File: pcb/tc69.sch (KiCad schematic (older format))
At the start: 99 parts, among them SW1 ESC, SW10 LWIN, SW11 2, SW12 W, SW13 S, SW14 Z, SW16 3, SW17 E, SW18 D, SW19 X, SW2 TAB, SW20 LALT, SW21 4, SW22 R, SW23 F, SW24 C, SW26 5, SW27 T, SW28 G, SW29 V, SW3 CAPS, SW30 LSPC, SW31 6, SW32 Y, SW33 H, SW34 B, SW36 7, SW37 U, SW38 J, SW39 N, SW4 LSHFT, SW41 8, SW42 I, SW43 K, SW44 M, SW45 RSPC, SW46 9, SW47 O, SW48 L, SW49 COMMA, SW5 LCTRL, SW51 0, SW52 P, SW53 SCLN, SW54 DOT, SW55 RALT, SW56 MINUS, SW57 LBRC, SW58 QUOTE, SW59 SLSH, SW6 1, SW60 RWIN, SW61 EQUAL, SW62 RBRC, SW65 APP, SW66 BS, SW68 ENTER, SW69 RSHFT, SW7 Q, SW70 LEFT, SW72 BSLSH, SW74 UP, SW75 DOWN, SW76 HOME, SW77 PGUP, SW78 PGDN, SW79 END, SW8 A, SW80 RIGHT, U1 SeeeduinoXIAO, U2 74AHC1G04, U3 NCS2003SN2T1G, U4 4051, U5 4051

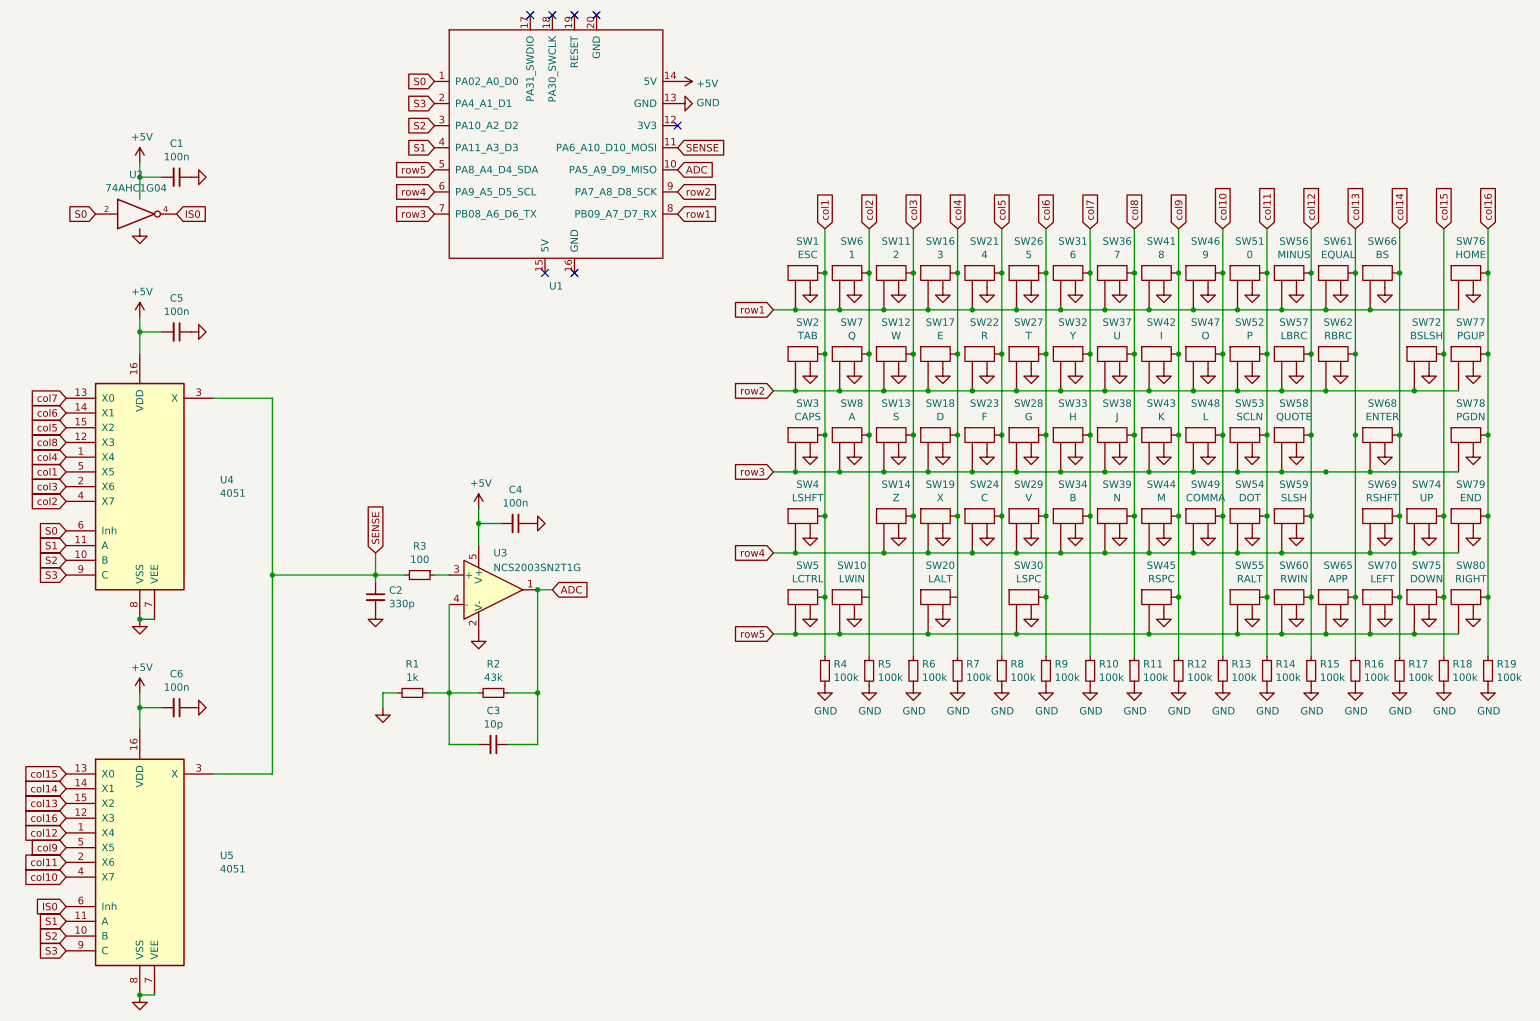
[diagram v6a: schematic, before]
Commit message: fix power line, made xiao rp2040 compatible
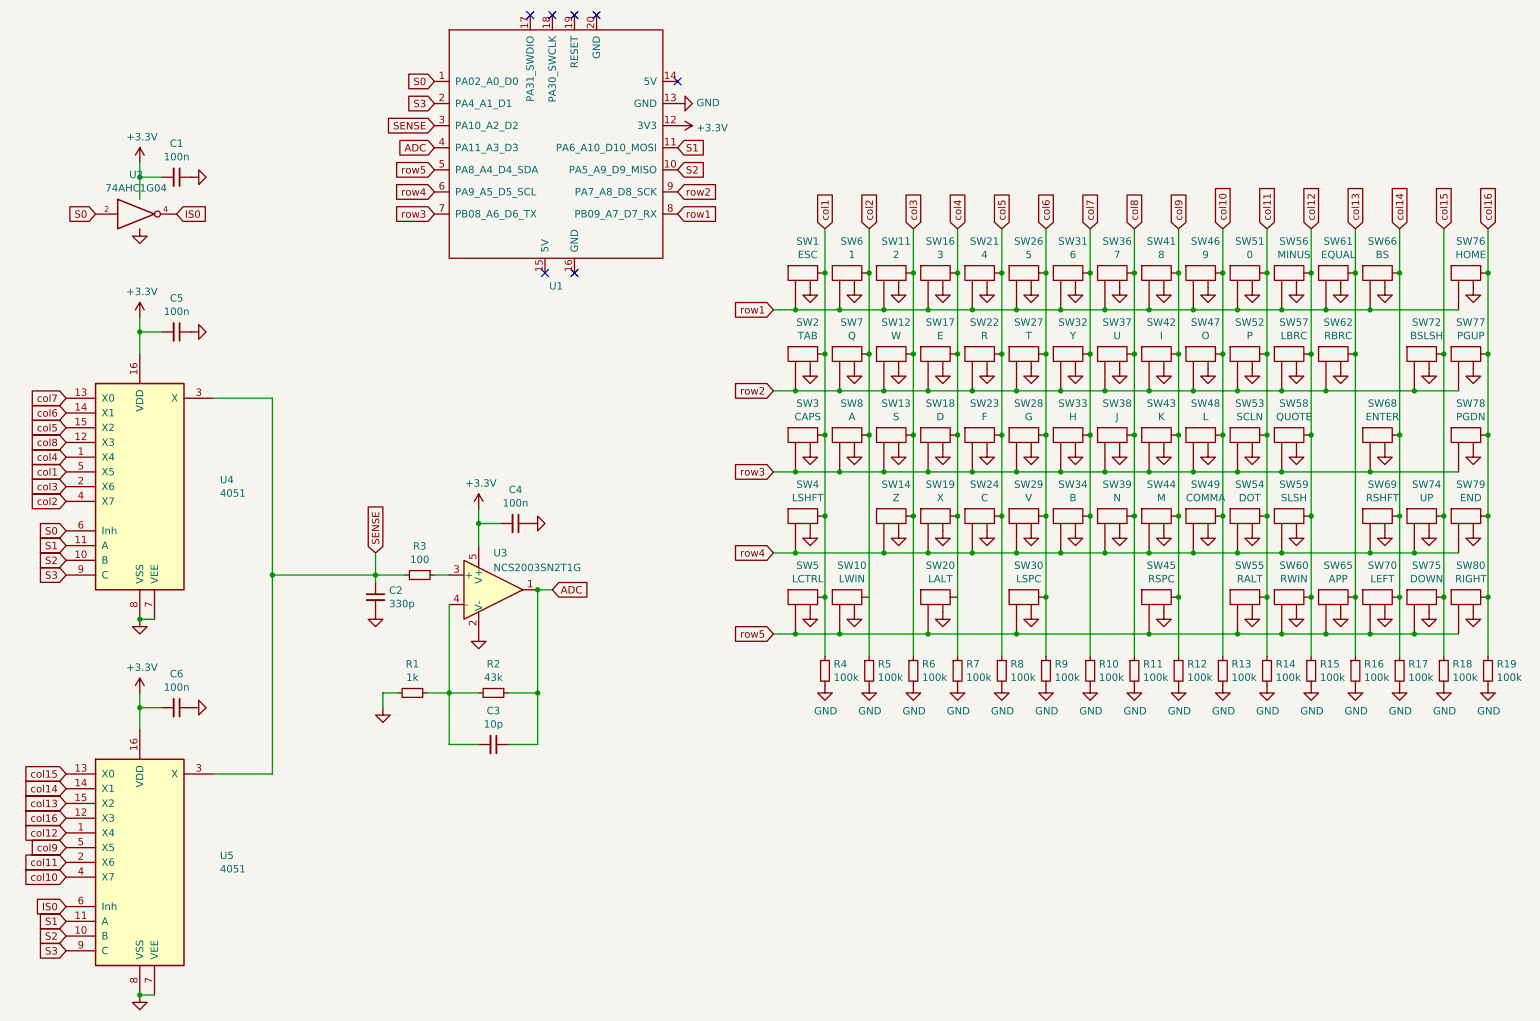
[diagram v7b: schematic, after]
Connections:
- net ADC: now also U1.4 (PA11_A3_D3); no longer U1.10 (PA5_A9_D9_MISO)
- net S1: now also U1.11 (PA6_A10_D10_MOSI); no longer U1.4 (PA11_A3_D3)
- net S2: now also U1.10 (PA5_A9_D9_MISO); no longer U1.3 (PA10_A2_D2)
- net SENSE: now also U1.3 (PA10_A2_D2); no longer U1.11 (PA6_A10_D10_MOSI)
- net +3V3: now reaches U1.12 (3V3)
- net +3V3: now also C1.2, C4.2, C5.2, C6.2, U2.5 (VCC), U3.5 (V+), U4.16 (VDD), U5.16 (VDD)
- removed net +5V: C1.2, C4.2, C5.2, C6.2, U1.14 (5V), U2.5 (VCC), U3.5 (V+), U4.16 (VDD), U5.16 (VDD)
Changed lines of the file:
@@
 	4150 5500 4150 4800
-$Comp
-L power:+5V #PWR0108
-U 1 1 61964144
-P 1450 1900
-F 0 "#PWR0108" H 1450 1750 50  0001 C CNN
-F 1 "+5V" H 1465 2073 50  0000 C CNN
-F 2 "" H 1450 1900 50  0001 C CNN
-F 3 "" H 1450 1900 50  0001 C CNN
-	1    1450 1900
-	1    0    0    -1
-$EndComp
 $Comp
 L Device:C_Small C1
@@
 NoConn ~ 4200 2650
 NoConn ~ 4400 2650
-$Comp
-L power:GND #PWR0110
-U 1 1 6198CF65
-P 5100 1500
-F 0 "#PWR0110" H 5100 1250 50  0001 C CNN
-F 1 "GND" V 5105 1372 50  0000 R CNN
-F 2 "" H 5100 1500 50  0001 C CNN
-F 3 "" H 5100 1500 50  0001 C CNN
-	1    5100 1500
-	0    -1   -1   0
-$EndComp
-$Comp
-L power:+5V #PWR0111
-U 1 1 6198D635
-P 5100 1350
-F 0 "#PWR0111" H 5100 1200 50  0001 C CNN
-F 1 "+5V" V 5115 1478 50  0000 L CNN
-F 2 "" H 5100 1350 50  0001 C CNN
-F 3 "" H 5100 1350 50  0001 C CNN
-	1    5100 1350
-	0    1    1    0
-$EndComp
-NoConn ~ 5100 1650
-Text GLabel 5100 1950 2    50   Input ~ 0
+Text GLabel 3450 1800 0    50   Input ~ 0
 ADC
-$Comp
-L Seeeduino_XIAO:SeeeduinoXIAO U1
-U 1 1 61932DBD
-P 4300 1800
-F 0 "U1" H 4275 861 50  0000 C CNN
-F 1 "SeeeduinoXIAO" H 4275 770 50  0001 C CNN
-F 2 "Seeeduino XIAO KICAD:Seeeduino XIAO-MOUDLE14P-2.54-21X17.8MM" H 3950 2000 50  0001 C CNN
-F 3 "" H 3950 2000 50  0001 C CNN
-	1    4300 1800
-	1    0    0    -1
-$EndComp
 Text GLabel 5100 2250 2    50   Input ~ 0
 row1
@@
 Text GLabel 3450 1350 0    50   Input ~ 0
 S0
-Text GLabel 3450 1800 0    50   Input ~ 0
+Text GLabel 5100 1800 2    50   Input ~ 0
 S1
-Text GLabel 3450 1650 0    50   Input ~ 0
+Text GLabel 5100 1950 2    50   Input ~ 0
 S2
 Text GLabel 3450 1500 0    50   Input ~ 0
 S3
-Text GLabel 5100 1800 2    50   Input ~ 0
+Text GLabel 3450 1650 0    50   Input ~ 0
 SENSE
 Text GLabel 950  6150 0    50   Input ~ 0
@@
 col1
 $Comp
-L power:+5V #PWR0102
-U 1 1 6197F28E
-P 1450 5500
-F 0 "#PWR0102" H 1450 5350 50  0001 C CNN
-F 1 "+5V" H 1465 5673 50  0000 C CNN
-F 2 "" H 1450 5500 50  0001 C CNN
-F 3 "" H 1450 5500 50  0001 C CNN
-	1    1450 5500
-	1    0    0    -1
-$EndComp
-$Comp
 L Device:C_Small C6
 U 1 1 6197F294
@@
 F 4 "C9386" H 1450 6650 50  0001 C CNN "LCSC"
 	1    1450 6650
-	1    0    0    -1
-$EndComp
-$Comp
-L power:+5V #PWR0198
-U 1 1 61A21E44
-P 1450 2950
-F 0 "#PWR0198" H 1450 2800 50  0001 C CNN
-F 1 "+5V" H 1465 3123 50  0000 C CNN
-F 2 "" H 1450 2950 50  0001 C CNN
-F 3 "" H 1450 2950 50  0001 C CNN
-	1    1450 2950
 	1    0    0    -1
 $EndComp
@@
 Wire Wire Line
 	6700 3750 6700 4300
-Wire Wire Line
-	9200 4000 9500 4000
-Wire Wire Line
-	9700 3200 9700 3750
 $Comp
 L power:GND #PWR0104
@@
 $EndComp
 $Comp
-L power:+5V #PWR0106
-U 1 1 6195DC54
-P 3750 4250
-F 0 "#PWR0106" H 3750 4100 50  0001 C CNN
-F 1 "+5V" H 3765 4423 50  0000 C CNN
-F 2 "" H 3750 4250 50  0001 C CNN
-F 3 "" H 3750 4250 50  0001 C CNN
-	1    3750 4250
-	1    0    0    -1
-$EndComp
-$Comp
 L Amplifier_Operational:NCS20071SN U3
 U 1 1 619B1295
@@
 	1    0    0    -1
 $EndComp
-Connection ~ 9500 4000
-Wire Wire Line
-	9500 4000 9800 4000
-Connection ~ 9700 3750
-Wire Wire Line
-	9700 3750 9700 4850
 Wire Wire Line
 	8900 4000 9200 4000
@@
 Wire Wire Line
 	6400 3750 6400 4850
+Wire Wire Line
+	9200 4000 9800 4000
+Wire Wire Line
+	9700 3200 9700 4850
+$Comp
+L Seeeduino_XIAO:SeeeduinoXIAO U1
+U 1 1 61932DBD
+P 4300 1800
+F 0 "U1" H 4275 861 50  0000 C CNN
+F 1 "SeeeduinoXIAO" H 4275 770 50  0001 C CNN
+F 2 "Seeeduino XIAO KICAD:Seeeduino XIAO-MOUDLE14P-2.54-21X17.8MM" H 3950 2000 50  0001 C CNN
+F 3 "" H 3950 2000 50  0001 C CNN
+	1    4300 1800
+	1    0    0    -1
+$EndComp
+$Comp
+L power:GND #PWR0110
+U 1 1 6198CF65
+P 5100 1500
+F 0 "#PWR0110" H 5100 1250 50  0001 C CNN
+F 1 "GND" V 5105 1372 50  0000 R CNN
+F 2 "" H 5100 1500 50  0001 C CNN
+F 3 "" H 5100 1500 50  0001 C CNN
+	1    5100 1500
+	0    -1   -1   0
+$EndComp
+NoConn ~ 5100 1350
+$Comp
+L power:+3.3V #PWR?
+U 1 1 61DFCB61
+P 5100 1650
+F 0 "#PWR?" H 5100 1500 50  0001 C CNN
+F 1 "+3.3V" V 5115 1778 50  0000 L CNN
+F 2 "" H 5100 1650 50  0001 C CNN
+F 3 "" H 5100 1650 50  0001 C CNN
+	1    5100 1650
+	0    1    1    0
+$EndComp
+$Comp
+L power:+3.3V #PWR?
+U 1 1 61DFE6EA
+P 1450 1900
+F 0 "#PWR?" H 1450 1750 50  0001 C CNN
+F 1 "+3.3V" H 1465 2073 50  0000 C CNN
+F 2 "" H 1450 1900 50  0001 C CNN
+F 3 "" H 1450 1900 50  0001 C CNN
+	1    1450 1900
+	1    0    0    -1
+$EndComp
+$Comp
+L power:+3.3V #PWR?
+U 1 1 61DFF73E
+P 1450 2950
+F 0 "#PWR?" H 1450 2800 50  0001 C CNN
+F 1 "+3.3V" H 1465 3123 50  0000 C CNN
+F 2 "" H 1450 2950 50  0001 C CNN
+F 3 "" H 1450 2950 50  0001 C CNN
+	1    1450 2950
+	1    0    0    -1
+$EndComp
+$Comp
+L power:+3.3V #PWR?
+U 1 1 61E00904
+P 1450 5500
+F 0 "#PWR?" H 1450 5350 50  0001 C CNN
+F 1 "+3.3V" H 1465 5673 50  0000 C CNN
+F 2 "" H 1450 5500 50  0001 C CNN
+F 3 "" H 1450 5500 50  0001 C CNN
+	1    1450 5500
+	1    0    0    -1
+$EndComp
+$Comp
+L power:+3.3V #PWR?
+U 1 1 61E018BB
+P 3750 4250
+F 0 "#PWR?" H 3750 4100 50  0001 C CNN
+F 1 "+3.3V" H 3765 4423 50  0000 C CNN
+F 2 "" H 3750 4250 50  0001 C CNN
+F 3 "" H 3750 4250 50  0001 C CNN
+	1    3750 4250
+	1    0    0    -1
+$EndComp
 $EndSCHEMATC

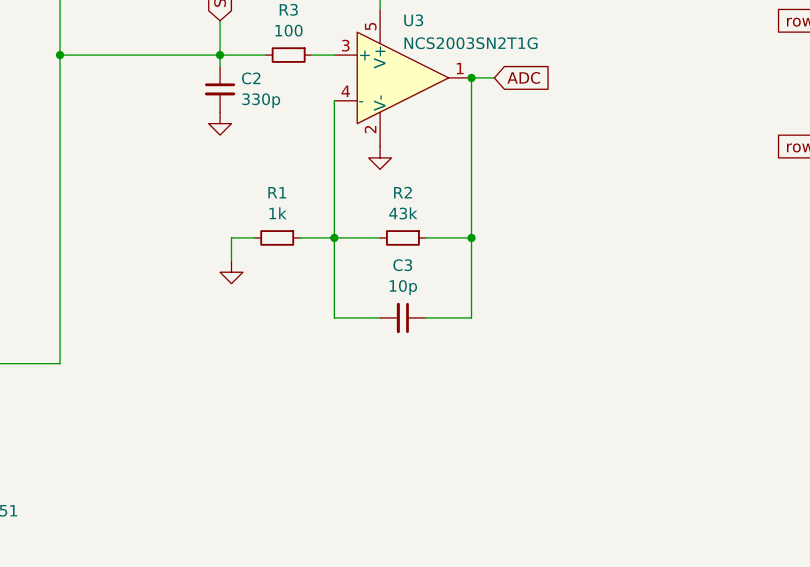
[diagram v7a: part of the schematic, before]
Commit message: fix op-amp output
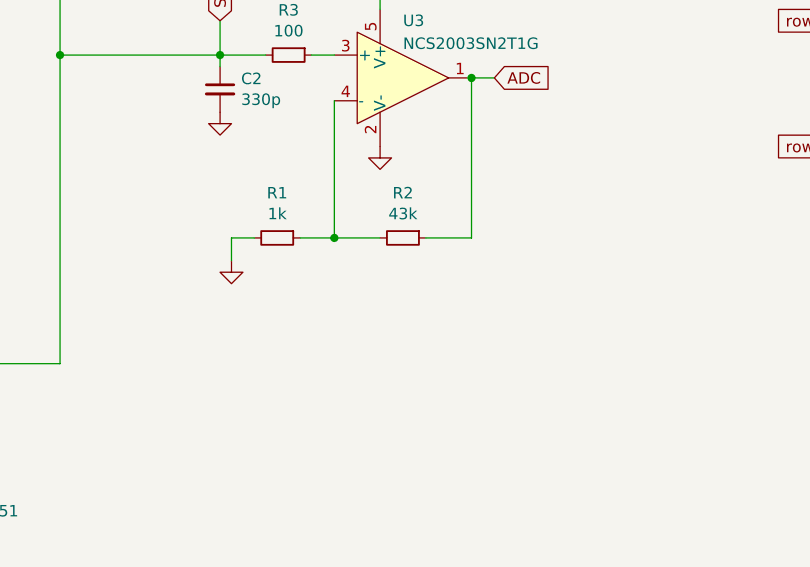
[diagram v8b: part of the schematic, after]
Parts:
- removed C3: 10p, Capacitor_SMD:C_0805_2012Metric_Pad1.18x1.45mm_HandSolder, symbol Device:C_Small
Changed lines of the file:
@@
 Wire Wire Line
 	3550 4900 3550 5500
-$Comp
-L Device:C_Small C3
-U 1 1 6195BD4C
-P 3850 5850
-F 0 "C3" V 3621 5850 50  0000 C CNN
-F 1 "10p" V 3712 5850 50  0000 C CNN
-F 2 "Capacitor_SMD:C_0805_2012Metric_Pad1.18x1.45mm_HandSolder" H 3850 5850 50  0001 C CNN
-F 3 "~" H 3850 5850 50  0001 C CNN
-F 4 "C157608" H 3850 5850 50  0001 C CNN "LCSC"
-	1    3850 5850
-	0    1    1    0
-$EndComp
-Wire Wire Line
-	3550 5500 3550 5850
-Wire Wire Line
-	3550 5850 3750 5850
-Wire Wire Line
-	3950 5850 4150 5850
-Wire Wire Line
-	4150 5850 4150 5500
 Wire Wire Line
 	3950 5500 4150 5500
-Connection ~ 4150 5500
 Wire Wire Line
 	4150 5500 4150 4800
